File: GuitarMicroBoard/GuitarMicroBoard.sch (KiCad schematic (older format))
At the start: 4 parts

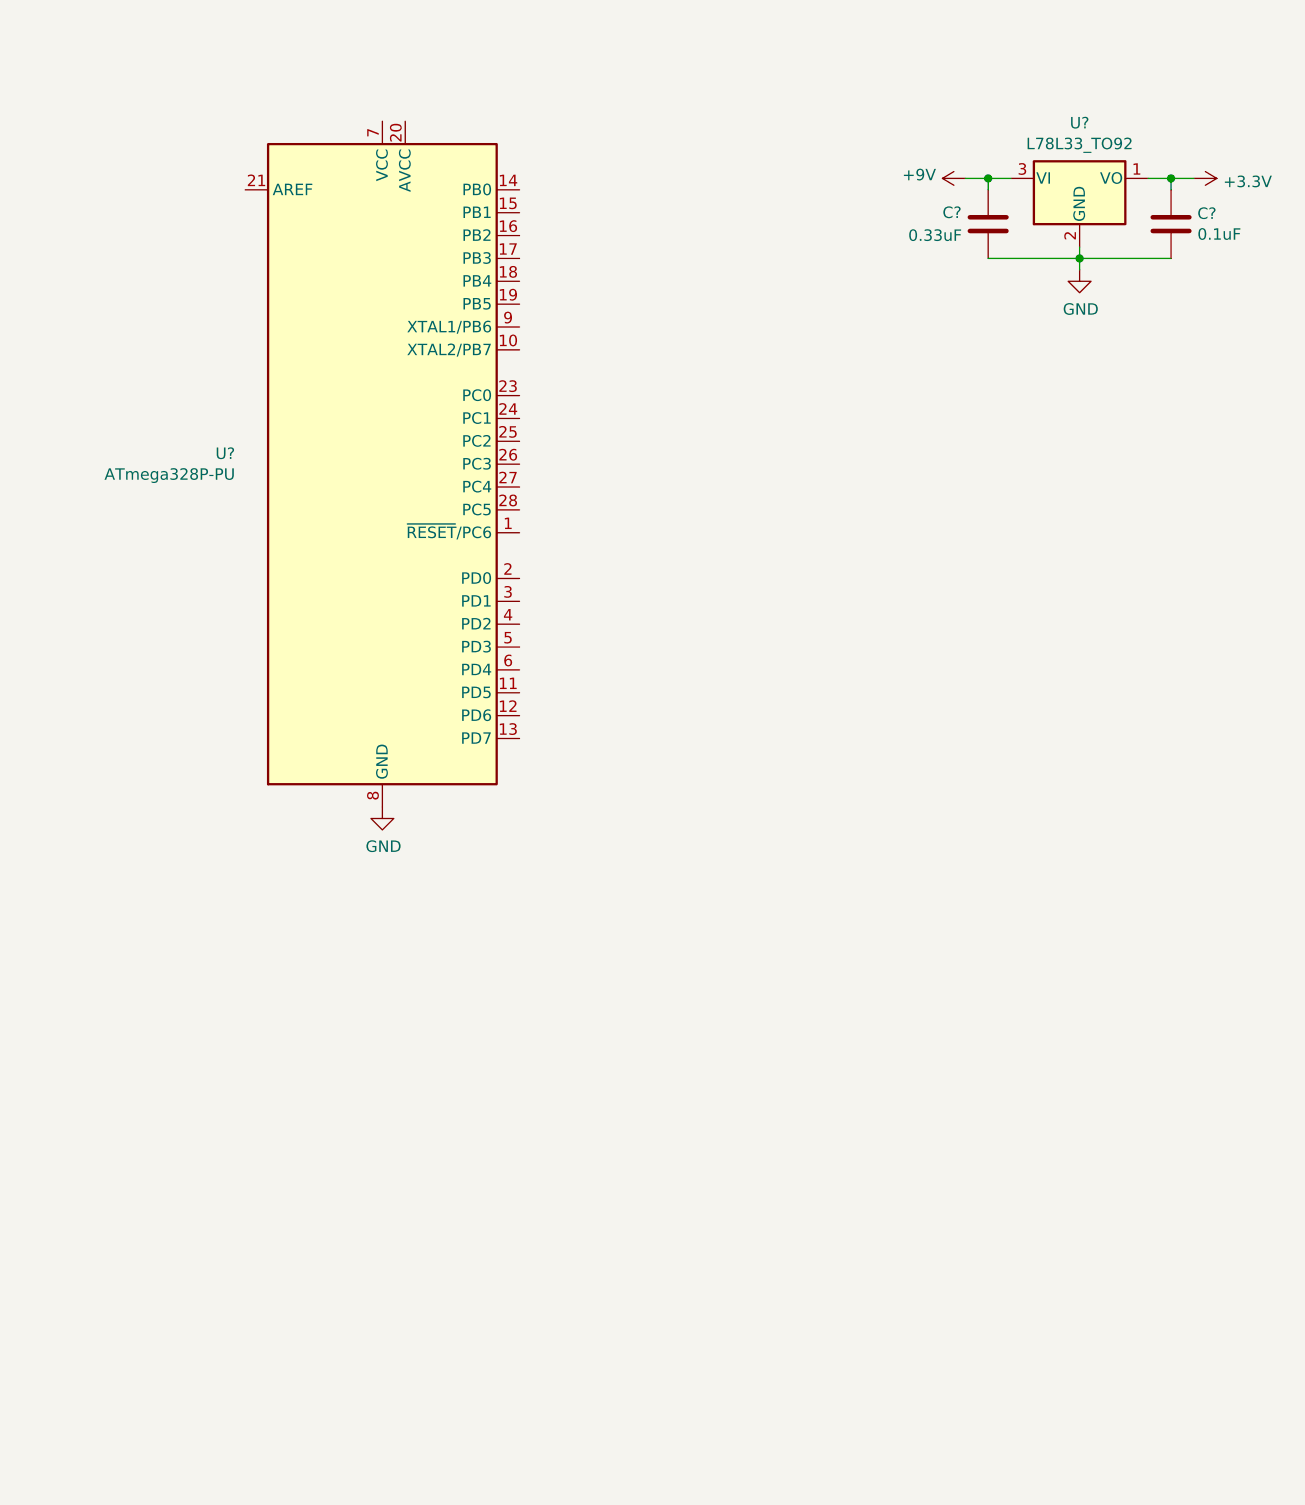
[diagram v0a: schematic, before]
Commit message: Trying to get everything to fit in the 3D printed pocket I've made
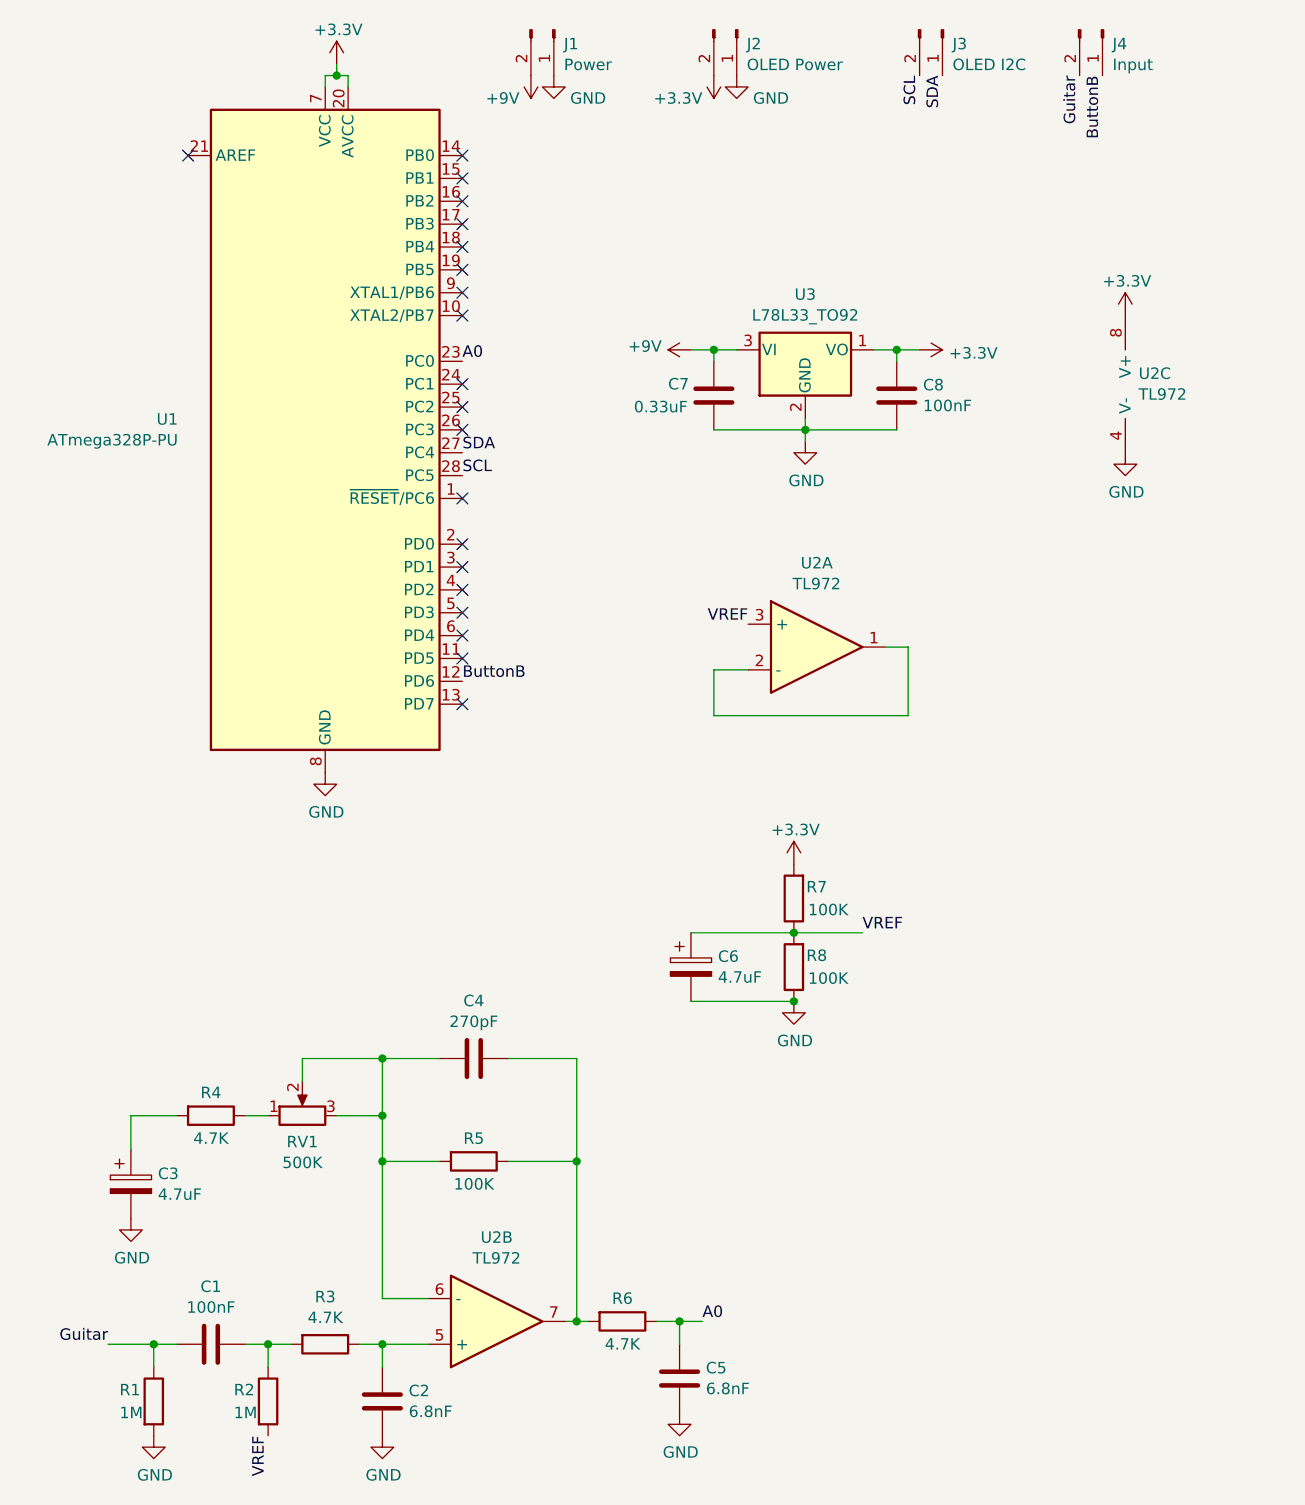
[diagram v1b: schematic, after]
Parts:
- added C1: 100nF, Capacitor_THT:C_Rect_L7.2mm_W2.5mm_P5.00mm_FKS2_FKP2_MKS2_MKP2, symbol Device:C
- added C2, C5: 6.8nF, Capacitor_THT:C_Rect_L7.2mm_W2.5mm_P5.00mm_FKS2_FKP2_MKS2_MKP2, symbol Device:C
- added C3, C6: 4.7uF, libraries:CP_Radial_D5.0mm_P2.00mm_L11.0mm, symbol Device:CP
- added C4: 270pF, Capacitor_THT:C_Rect_L7.2mm_W2.5mm_P5.00mm_FKS2_FKP2_MKS2_MKP2, symbol Device:C
- added J1: Power, Connector_PinSocket_2.54mm:PinSocket_1x02_P2.54mm_Vertical, symbol Connector:Conn_01x02_Male
- added J2: OLED Power, TerminalBlock:TerminalBlock_bornier-2_P5.08mm, symbol Connector:Conn_01x02_Male
- added J3: OLED I2C, TerminalBlock:TerminalBlock_bornier-2_P5.08mm, symbol Connector:Conn_01x02_Male
- added J4: Input, TerminalBlock:TerminalBlock_bornier-2_P5.08mm, symbol Connector:Conn_01x02_Male
- added R1, R2: 1M, Resistor_THT:R_Axial_DIN0207_L6.3mm_D2.5mm_P10.16mm_Horizontal, symbol Device:R
- added R3, R4, R6: 4.7K, Resistor_THT:R_Axial_DIN0207_L6.3mm_D2.5mm_P10.16mm_Horizontal, symbol Device:R
- added R5, R7, R8: 100K, Resistor_THT:R_Axial_DIN0207_L6.3mm_D2.5mm_P10.16mm_Horizontal, symbol Device:R
- added RV1: 500K, Potentiometer_THT:Potentiometer_Bourns_3386F_Vertical, symbol Device:R_POT
- added U2: TL972, Package_DIP:DIP-8_W7.62mm, symbol Device:Opamp_Dual_Generic
- C7: renamed from C?; footprint (none) -> Capacitor_THT:C_Rect_L7.2mm_W2.5mm_P5.00mm_FKS2_FKP2_MKS2_MKP2
- C8: renamed from C?; value 0.1uF -> 100nF; footprint (none) -> Capacitor_THT:C_Rect_L7.2mm_W2.5mm_P5.00mm_FKS2_FKP2_MKS2_MKP2
- gave numbers to parts that had none: 2
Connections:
- net +3V3: now also U1.20 (AVCC), U1.7 (VCC), J2.2 (Pin_2), R7.2, U2.8 (V+)
- net +9V: now also J1.2 (Pin_2)
- net GND: now also C2.1, C3.2, C5.2, C6.2, J1.1 (Pin_1), J2.1 (Pin_1), R1.2, R8.1, U2.4 (V-)
- net ButtonB: now reaches U1.12 (PD6)
- net ButtonB: now also J4.1 (Pin_1)
- net A0: now reaches U1.23 (PC0)
- net A0: now also C5.1, R6.1
- net SDA: now reaches U1.27 (PC4)
- net SDA: now also J3.1 (Pin_1)
- net SCL: now reaches U1.28 (PC5)
- net SCL: now also J3.2 (Pin_2)
- new net: C1.1, R2.1, R3.2
- new net: C2.2, R3.1, U2.5 (+)
- new net: U2.1, U2.2 (-)
- new net: C4.1, R5.2, RV1.2, RV1.3, U2.6 (-)
- new net: C4.2, R5.1, R6.2, U2.7
- new net: R4.1, RV1.1
- new net: C3.1, R4.2
- new net Guitar: C1.2, J4.2 (Pin_2), R1.1
- new net VREF: C6.1, R2.2, R7.1, R8.2, U2.3 (+)
- no-connect marks 0 -> 20
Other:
- moved on the sheet: C7, C8, U1, U3
